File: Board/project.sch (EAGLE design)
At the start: 19 parts, among them U1 ATMEGA328P_PDIP

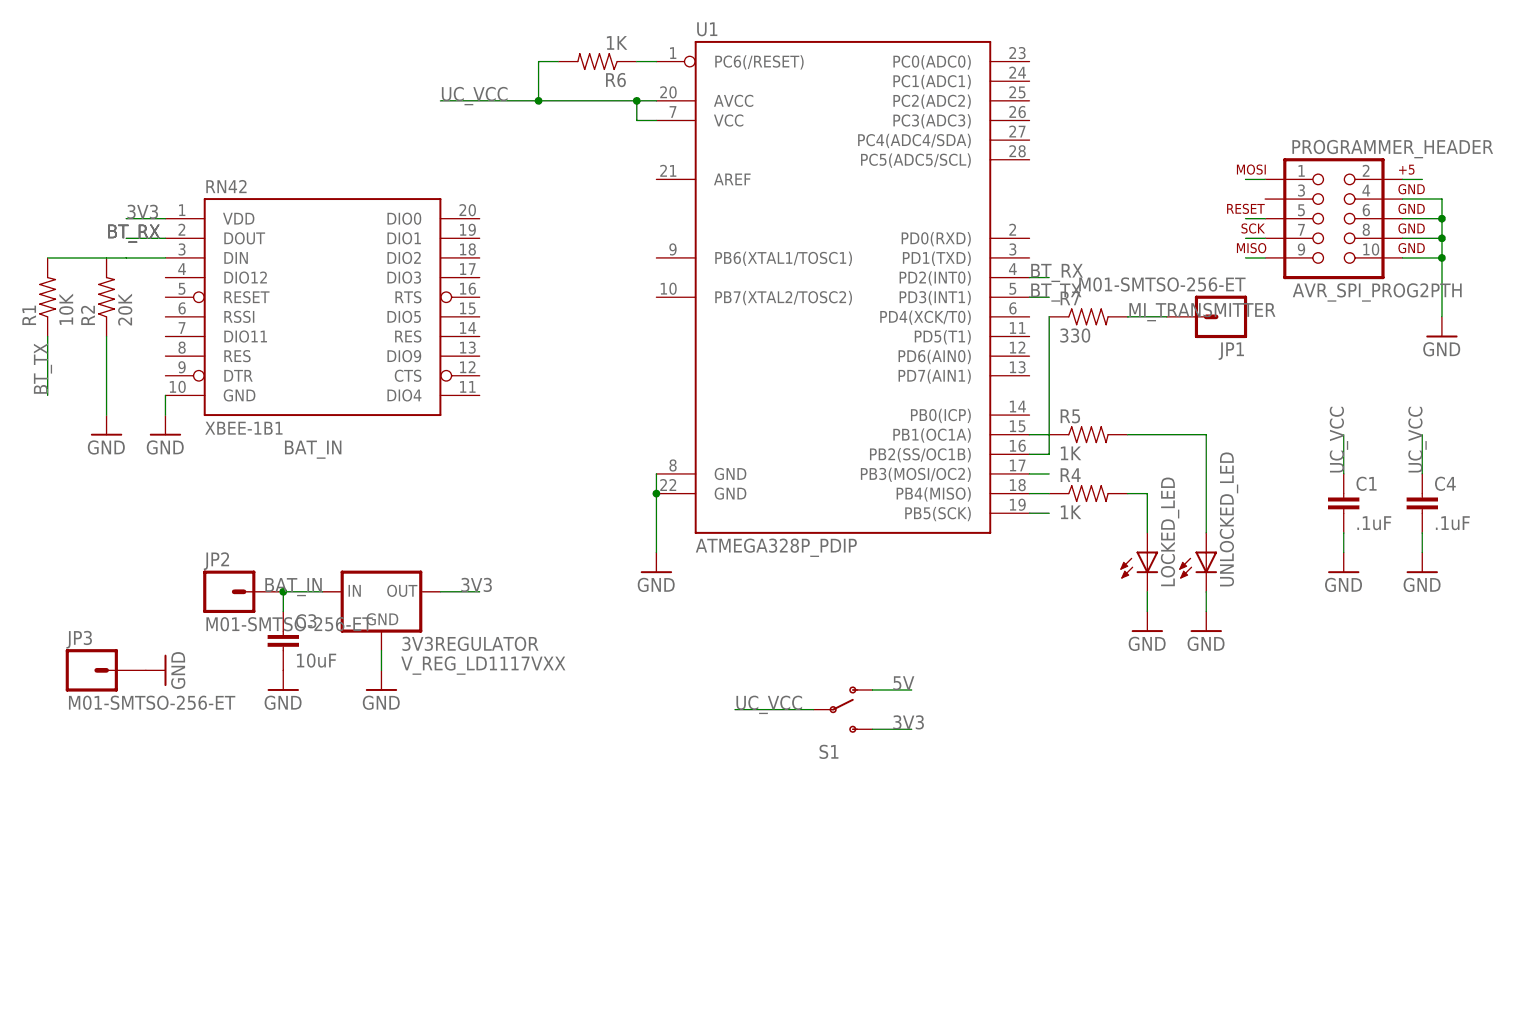
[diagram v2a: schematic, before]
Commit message: Better board layout, everything that needs to be should be connected, passes DRC.
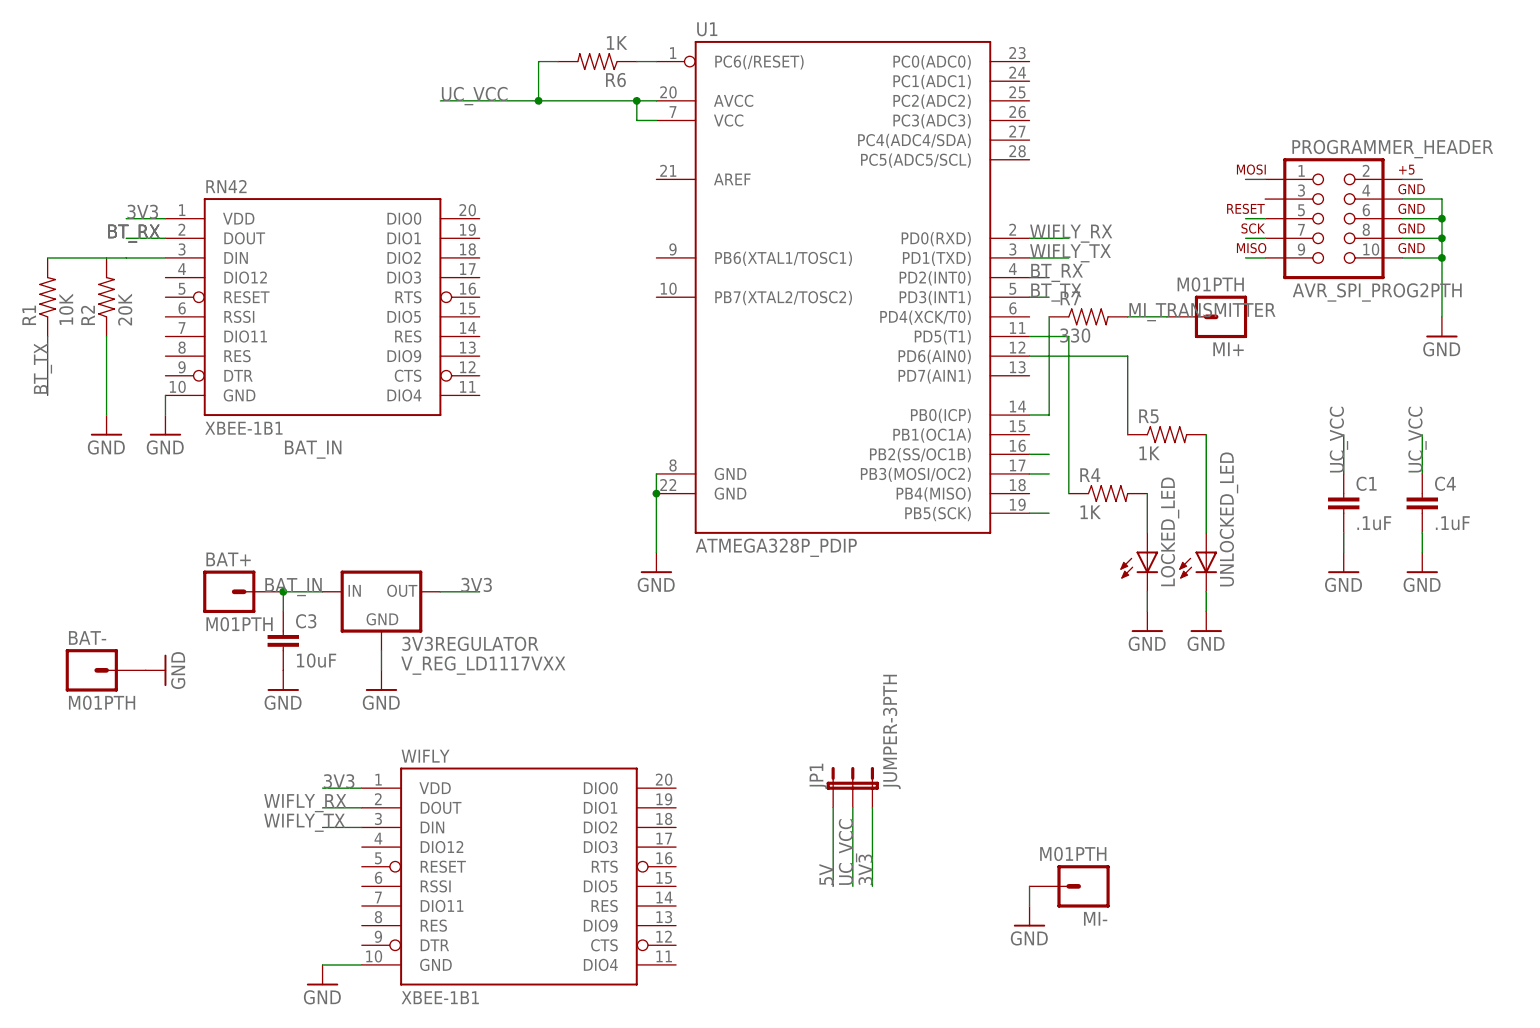
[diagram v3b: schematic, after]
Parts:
- removed JP2, JP3: M01-SMTSO-256-ET, SparkFun-Connectors:M01-SMTSO-256-ET
- removed S1: (no value), SparkFun-Electromechanical:SWITCH-SPDTPTH
- added BAT+, BAT-, MI+, MI-: M01PTH, SparkFun-Connectors:M01PTH
- added WIFLY: XBEE-1B1, SparkFun-RF:XBEE-1B1
- JP1: value M01-SMTSO-256-ET -> JUMPER-3PTH; device SparkFun-Connectors:M01-SMTSO-256-ET -> SparkFun-Passives:JUMPER-3PTH
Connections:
- new net N$4: R4.1, U1.PD5(T1)
- new net N$7: R7.1, U1.PB0(ICP)
- new net WIFLY_RX: U1.PD0(RXD), WIFLY.DOUT
- new net WIFLY_TX: U1.PD1(TXD), WIFLY.DIN
- net 3V3: now also JP1.3, WIFLY.VDD; no longer S1.S
- net 5V: now also JP1.1; no longer S1.O
- net BAT_IN: now also BAT+.1; no longer JP2.1
- net GND: now also BAT-.1, MI-.1, WIFLY.GND; no longer JP3.1
- net MISO: no longer R4.1, U1.PB4(MISO)
- net MI_TRANSMITTER: now also MI+.1; no longer JP1.1
- net N$2: now also U1.PD6(AIN0); no longer U1.PB1(OC1A)
- net N$3: no longer R7.1
- net UC_VCC: no longer S1.P
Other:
- moved on the sheet: R4, R5
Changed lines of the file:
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@@
 <part name="UNLOCKED_LED" library="SparkFun-LED" deviceset="LED" device="5MM"/>
 <part name="LOCKED_LED" library="SparkFun-LED" deviceset="LED" device="5MM"/>
-<part name="S1" library="SparkFun-Electromechanical" deviceset="SWITCH-SPDT" device="PTH"/>
 <part name="GND1" library="SparkFun-Aesthetics" deviceset="GND" device=""/>
 <part name="GND2" library="SparkFun-Aesthetics" deviceset="GND" device=""/>
@@
 <part name="GND9" library="SparkFun-Aesthetics" deviceset="GND" device=""/>
 <part name="GND10" library="SparkFun-Aesthetics" deviceset="GND" device=""/>
-<part name="JP1" library="SparkFun-Connectors" deviceset="M01" device="-SMTSO-256-ET"/>
-<part name="JP2" library="SparkFun-Connectors" deviceset="M01" device="-SMTSO-256-ET"/>
-<part name="JP3" library="SparkFun-Connectors" deviceset="M01" device="-SMTSO-256-ET"/>
 <part name="GND11" library="SparkFun-Aesthetics" deviceset="GND" device=""/>
+<part name="WIFLY" library="SparkFun-RF" deviceset="XBEE-1" device="B1"/>
+<part name="GND12" library="SparkFun-Aesthetics" deviceset="GND" device=""/>
+<part name="BAT+" library="SparkFun-Connectors" deviceset="M01" device="PTH"/>
+<part name="MI+" library="SparkFun-Connectors" deviceset="M01" device="PTH"/>
+<part name="BAT-" library="SparkFun-Connectors" deviceset="M01" device="PTH"/>
+<part name="JP1" library="SparkFun-Passives" deviceset="JUMPER-3" device="PTH"/>
+<part name="MI-" library="SparkFun-Connectors" deviceset="M01" device="PTH"/>
+<part name="GND13" library="SparkFun-Aesthetics" deviceset="GND" device=""/>
 </parts>
 <sheets>
@@
 <instance part="R1" gate="G$1" x="-96.52" y="91.44" rot="R90"/>
 <instance part="R2" gate="G$1" x="-88.9" y="91.44" rot="R90"/>
-<instance part="R4" gate="G$1" x="38.1" y="66.04"/>
-<instance part="R5" gate="G$1" x="38.1" y="73.66"/>
+<instance part="R4" gate="G$1" x="40.64" y="66.04"/>
+<instance part="R5" gate="G$1" x="48.26" y="73.66"/>
 <instance part="R6" gate="G$1" x="-25.4" y="121.92" rot="R180"/>
 <instance part="C1" gate="G$1" x="71.12" y="63.5"/>
@@
 <instance part="UNLOCKED_LED" gate="G$1" x="53.34" y="58.42"/>
 <instance part="LOCKED_LED" gate="G$1" x="45.72" y="58.42"/>
-<instance part="S1" gate="1" x="5.08" y="38.1"/>
 <instance part="GND1" gate="1" x="-17.78" y="55.88"/>
 <instance part="GND2" gate="1" x="-53.34" y="40.64"/>
@@
 <instance part="GND9" gate="1" x="81.28" y="55.88"/>
 <instance part="GND10" gate="1" x="-66.04" y="40.64"/>
-<instance part="JP1" gate="G$1" x="55.88" y="88.9" rot="R180"/>
-<instance part="JP2" gate="G$1" x="-73.66" y="53.34"/>
-<instance part="JP3" gate="G$1" x="-91.44" y="43.18"/>
 <instance part="GND11" gate="1" x="-81.28" y="43.18" rot="R90"/>
+<instance part="WIFLY" gate="G$1" x="-35.56" y="17.78"/>
+<instance part="GND12" gate="1" x="-60.96" y="2.54"/>
+<instance part="BAT+" gate="G$1" x="-73.66" y="53.34"/>
+<instance part="MI+" gate="G$1" x="55.88" y="88.9" rot="R180"/>
+<instance part="BAT-" gate="G$1" x="-91.44" y="43.18"/>
+<instance part="JP1" gate="G$1" x="5.08" y="27.94"/>
+<instance part="MI-" gate="G$1" x="38.1" y="15.24" rot="R180"/>
+<instance part="GND13" gate="1" x="30.48" y="10.16"/>
 </instances>
 <busses>
@@
 </segment>
 <segment>
-<pinref part="JP3" gate="G$1" pin="1"/>
+<pinref part="WIFLY" gate="G$1" pin="GND"/>
+<wire x1="-55.88" y1="5.08" x2="-60.96" y2="5.08" width="0.1524" layer="91"/>
+<pinref part="GND12" gate="1" pin="GND"/>
+</segment>
+<segment>
 <pinref part="GND11" gate="1" pin="GND"/>
+<pinref part="BAT-" gate="G$1" pin="1"/>
+</segment>
+<segment>
+<pinref part="MI-" gate="G$1" pin="1"/>
+<pinref part="GND13" gate="1" pin="GND"/>
+<wire x1="30.48" y1="15.24" x2="30.48" y2="12.7" width="0.1524" layer="91"/>
 </segment>
 </net>
 <net name="UC_VCC" class="0">
 <segment>
-<pinref part="S1" gate="1" pin="P"/>
-<label x="-7.62" y="38.1" size="1.778" layer="95"/>
-<wire x1="2.54" y1="38.1" x2="-7.62" y2="38.1" width="0.1524" layer="91"/>
+<label x="7.62" y="15.24" size="1.778" layer="95" rot="R90"/>
+<wire x1="7.62" y1="25.4" x2="7.62" y2="15.24" width="0.1524" layer="91"/>
 </segment>
 <segment>
@@
 <net name="5V" class="0">
 <segment>
-<pinref part="S1" gate="1" pin="O"/>
-<wire x1="10.16" y1="40.64" x2="15.24" y2="40.64" width="0.1524" layer="91"/>
-<label x="12.7" y="40.64" size="1.778" layer="95"/>
-</segment>
-<segment>
 <pinref part="PROGRAMMER_HEADER" gate="A" pin="2"/>
 <wire x1="78.74" y1="106.68" x2="81.28" y2="106.68" width="0.1524" layer="91"/>
 </segment>
+<segment>
+<pinref part="JP1" gate="G$1" pin="1"/>
+<wire x1="5.08" y1="25.4" x2="5.08" y2="15.24" width="0.1524" layer="91"/>
+<label x="5.08" y="15.24" size="1.778" layer="95" rot="R90"/>
+</segment>
 </net>
 <net name="3V3" class="0">
-<segment>
-<pinref part="S1" gate="1" pin="S"/>
-<wire x1="10.16" y1="35.56" x2="15.24" y2="35.56" width="0.1524" layer="91"/>
-<label x="12.7" y="35.56" size="1.778" layer="95"/>
-</segment>
 <segment>
 <pinref part="3V3REGULATOR" gate="G$1" pin="OUT"/>
@@
 <label x="-86.36" y="101.6" size="1.778" layer="95"/>
 <wire x1="-81.28" y1="101.6" x2="-86.36" y2="101.6" width="0.1524" layer="91"/>
+</segment>
+<segment>
+<pinref part="WIFLY" gate="G$1" pin="VDD"/>
+<wire x1="-55.88" y1="27.94" x2="-60.96" y2="27.94" width="0.1524" layer="91"/>
+<label x="-60.96" y="27.94" size="1.778" layer="95"/>
+</segment>
+<segment>
+<pinref part="JP1" gate="G$1" pin="3"/>
+<wire x1="10.16" y1="25.4" x2="10.16" y2="15.24" width="0.1524" layer="91"/>
+<label x="10.16" y="15.24" size="1.778" layer="95" rot="R90"/>
 </segment>
 </net>
@@
 <label x="-66.04" y="71.12" size="1.778" layer="95"/>
 <label x="-68.58" y="53.34" size="1.778" layer="95"/>
-<pinref part="JP2" gate="G$1" pin="1"/>
+<pinref part="BAT+" gate="G$1" pin="1"/>
 <junction x="-66.04" y="53.34"/>
 </segment>
 </net>
 <net name="MISO" class="0">
-<segment>
-<pinref part="U1" gate="G$1" pin="PB4(MISO)"/>
-<pinref part="R4" gate="G$1" pin="1"/>
-<wire x1="30.48" y1="66.04" x2="33.02" y2="66.04" width="0.1524" layer="91"/>
-</segment>
 <segment>
 <pinref part="PROGRAMMER_HEADER" gate="A" pin="9"/>
@@
 <segment>
 <pinref part="R4" gate="G$1" pin="2"/>
-<wire x1="43.18" y1="66.04" x2="45.72" y2="66.04" width="0.1524" layer="91"/>
 <pinref part="LOCKED_LED" gate="G$1" pin="A"/>
 <wire x1="45.72" y1="66.04" x2="45.72" y2="60.96" width="0.1524" layer="91"/>
@@
 <segment>
 <pinref part="R5" gate="G$1" pin="2"/>
-<wire x1="43.18" y1="73.66" x2="53.34" y2="73.66" width="0.1524" layer="91"/>
 <pinref part="UNLOCKED_LED" gate="G$1" pin="A"/>
 <wire x1="53.34" y1="73.66" x2="53.34" y2="60.96" width="0.1524" layer="91"/>
@@
 <wire x1="43.18" y1="88.9" x2="48.26" y2="88.9" width="0.1524" layer="91"/>
 <label x="43.18" y="88.9" size="1.778" layer="95"/>
-<pinref part="JP1" gate="G$1" pin="1"/>
-</segment>
-</net>
-<net name="N$2" class="0">
-<segment>
-<pinref part="U1" gate="G$1" pin="PB1(OC1A)"/>
-<pinref part="R5" gate="G$1" pin="1"/>
-<wire x1="30.48" y1="73.66" x2="33.02" y2="73.66" width="0.1524" layer="91"/>
+<pinref part="MI+" gate="G$1" pin="1"/>
 </segment>
 </net>
@@
 <pinref part="U1" gate="G$1" pin="PB2(SS/OC1B)"/>
 <wire x1="30.48" y1="71.12" x2="33.02" y2="71.12" width="0.1524" layer="91"/>
+</segment>
+</net>
+<net name="WIFLY_RX" class="0">
+<segment>
+<pinref part="WIFLY" gate="G$1" pin="DOUT"/>
+<wire x1="-55.88" y1="25.4" x2="-60.96" y2="25.4" width="0.1524" layer="91"/>
+<label x="-68.58" y="25.4" size="1.778" layer="95"/>
+</segment>
+<segment>
+<pinref part="U1" gate="G$1" pin="PD0(RXD)"/>
+<wire x1="30.48" y1="99.06" x2="35.56" y2="99.06" width="0.1524" layer="91"/>
+<label x="30.48" y="99.06" size="1.778" layer="95"/>
+</segment>
+</net>
+<net name="WIFLY_TX" class="0">
+<segment>
+<pinref part="WIFLY" gate="G$1" pin="DIN"/>
+<wire x1="-55.88" y1="22.86" x2="-60.96" y2="22.86" width="0.1524" layer="91"/>
+<label x="-68.58" y="22.86" size="1.778" layer="95"/>
+</segment>
+<segment>
+<pinref part="U1" gate="G$1" pin="PD1(TXD)"/>
+<wire x1="30.48" y1="96.52" x2="35.56" y2="96.52" width="0.1524" layer="91"/>
+<label x="30.48" y="96.52" size="1.778" layer="95"/>
+</segment>
+</net>
+<net name="N$2" class="0">
+<segment>
+<pinref part="U1" gate="G$1" pin="PD6(AIN0)"/>
+<wire x1="30.48" y1="83.82" x2="43.18" y2="83.82" width="0.1524" layer="91"/>
+<pinref part="R5" gate="G$1" pin="1"/>
+<wire x1="43.18" y1="83.82" x2="43.18" y2="73.66" width="0.1524" layer="91"/>
+</segment>
+</net>
+<net name="N$4" class="0">
+<segment>
+<pinref part="R4" gate="G$1" pin="1"/>
+<wire x1="35.56" y1="66.04" x2="35.56" y2="86.36" width="0.1524" layer="91"/>
+<pinref part="U1" gate="G$1" pin="PD5(T1)"/>
+<wire x1="35.56" y1="86.36" x2="30.48" y2="86.36" width="0.1524" layer="91"/>
+</segment>
+</net>
+<net name="N$7" class="0">
+<segment>
+<pinref part="U1" gate="G$1" pin="PB0(ICP)"/>
+<wire x1="30.48" y1="76.2" x2="33.02" y2="76.2" width="0.1524" layer="91"/>
 <pinref part="R7" gate="G$1" pin="1"/>
-<wire x1="33.02" y1="71.12" x2="33.02" y2="88.9" width="0.1524" layer="91"/>
-</segment>
-</net>
+<wire x1="33.02" y1="76.2" x2="33.02" y2="88.9" width="0.1524" layer="91"/>
+</segment>
+</net>

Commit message: Layout actually works, added silkscreen.
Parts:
- removed JP1: JUMPER-3PTH, SparkFun-Passives:JUMPER-3PTH
- added JP2: JUMPER-3-OLDPTH, SparkFun-Passives:JUMPER-3-OLDPTH
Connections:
- net 3V3: now also 3V3REGULATOR.IN, JP2.1; no longer 3V3REGULATOR.OUT, JP1.3
- net 5V: now also JP2.3; no longer JP1.1
- net BAT_IN: now also 3V3REGULATOR.GND; no longer 3V3REGULATOR.IN
- net GND: now also 3V3REGULATOR.OUT; no longer 3V3REGULATOR.GND
- net UC_VCC: now also JP2.2
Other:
- moved on the sheet: 3V3REGULATOR
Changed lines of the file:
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@@
 <part name="MI+" library="SparkFun-Connectors" deviceset="M01" device="PTH"/>
 <part name="BAT-" library="SparkFun-Connectors" deviceset="M01" device="PTH"/>
-<part name="JP1" library="SparkFun-Passives" deviceset="JUMPER-3" device="PTH"/>
 <part name="MI-" library="SparkFun-Connectors" deviceset="M01" device="PTH"/>
 <part name="GND13" library="SparkFun-Aesthetics" deviceset="GND" device=""/>
+<part name="JP2" library="SparkFun-Passives" deviceset="JUMPER-3-OLD" device="PTH"/>
 </parts>
 <sheets>
@@
 <instance part="PROGRAMMER_HEADER" gate="A" x="68.58" y="101.6"/>
 <instance part="RN42" gate="G$1" x="-60.96" y="91.44"/>
-<instance part="3V3REGULATOR" gate="G$1" x="-53.34" y="53.34"/>
+<instance part="3V3REGULATOR" gate="G$1" x="-55.88" y="55.88" rot="R90"/>
 <instance part="R1" gate="G$1" x="-96.52" y="91.44" rot="R90"/>
 <instance part="R2" gate="G$1" x="-88.9" y="91.44" rot="R90"/>
@@
 <instance part="MI+" gate="G$1" x="55.88" y="88.9" rot="R180"/>
 <instance part="BAT-" gate="G$1" x="-91.44" y="43.18"/>
-<instance part="JP1" gate="G$1" x="5.08" y="27.94"/>
 <instance part="MI-" gate="G$1" x="38.1" y="15.24" rot="R180"/>
 <instance part="GND13" gate="1" x="30.48" y="10.16"/>
+<instance part="JP2" gate="G$1" x="-7.62" y="30.48"/>
 </instances>
 <busses>
@@
 <junction x="-17.78" y="66.04"/>
 <pinref part="GND1" gate="1" pin="GND"/>
-</segment>
-<segment>
-<pinref part="3V3REGULATOR" gate="G$1" pin="GND"/>
-<pinref part="GND2" gate="1" pin="GND"/>
-<wire x1="-53.34" y1="43.18" x2="-53.34" y2="45.72" width="0.1524" layer="91"/>
 </segment>
 <segment>
@@
 <wire x1="30.48" y1="15.24" x2="30.48" y2="12.7" width="0.1524" layer="91"/>
 </segment>
+<segment>
+<pinref part="GND2" gate="1" pin="GND"/>
+<wire x1="-53.34" y1="43.18" x2="-43.18" y2="53.34" width="0.1524" layer="91"/>
+<wire x1="-43.18" y1="53.34" x2="-43.18" y2="63.5" width="0.1524" layer="91"/>
+<pinref part="3V3REGULATOR" gate="G$1" pin="OUT"/>
+<wire x1="-43.18" y1="63.5" x2="-55.88" y2="63.5" width="0.1524" layer="91"/>
+</segment>
 </net>
 <net name="UC_VCC" class="0">
-<segment>
-<label x="7.62" y="15.24" size="1.778" layer="95" rot="R90"/>
-<wire x1="7.62" y1="25.4" x2="7.62" y2="15.24" width="0.1524" layer="91"/>
-</segment>
 <segment>
 <pinref part="U1" gate="G$1" pin="AVCC"/>
@@
 <label x="81.28" y="68.58" size="1.778" layer="95" rot="R90"/>
 </segment>
+<segment>
+<pinref part="JP2" gate="G$1" pin="2"/>
+<wire x1="-5.08" y1="27.94" x2="-5.08" y2="20.32" width="0.1524" layer="91"/>
+<label x="-5.08" y="17.78" size="1.778" layer="95" rot="R90"/>
+</segment>
 </net>
 <net name="5V" class="0">
@@
 </segment>
 <segment>
-<pinref part="JP1" gate="G$1" pin="1"/>
-<wire x1="5.08" y1="25.4" x2="5.08" y2="15.24" width="0.1524" layer="91"/>
-<label x="5.08" y="15.24" size="1.778" layer="95" rot="R90"/>
+<pinref part="JP2" gate="G$1" pin="3"/>
+<wire x1="-2.54" y1="27.94" x2="-2.54" y2="20.32" width="0.1524" layer="91"/>
+<label x="-2.54" y="22.86" size="1.778" layer="95" rot="R90"/>
 </segment>
 </net>
 <net name="3V3" class="0">
-<segment>
-<pinref part="3V3REGULATOR" gate="G$1" pin="OUT"/>
-<wire x1="-45.72" y1="53.34" x2="-40.64" y2="53.34" width="0.1524" layer="91"/>
-<label x="-43.18" y="53.34" size="1.778" layer="95"/>
-</segment>
 <segment>
 <pinref part="RN42" gate="G$1" pin="VDD"/>
@@
 </segment>
 <segment>
-<pinref part="JP1" gate="G$1" pin="3"/>
-<wire x1="10.16" y1="25.4" x2="10.16" y2="15.24" width="0.1524" layer="91"/>
-<label x="10.16" y="15.24" size="1.778" layer="95" rot="R90"/>
+<pinref part="JP2" gate="G$1" pin="1"/>
+<wire x1="-7.62" y1="27.94" x2="-7.62" y2="20.32" width="0.1524" layer="91"/>
+<label x="-7.62" y="22.86" size="1.778" layer="95" rot="R90"/>
+</segment>
+<segment>
+<pinref part="3V3REGULATOR" gate="G$1" pin="IN"/>
+<wire x1="-55.88" y1="45.72" x2="-55.88" y2="48.26" width="0.1524" layer="91"/>
+<label x="-55.88" y="45.72" size="1.778" layer="95" rot="R90"/>
 </segment>
 </net>
 <net name="BAT_IN" class="0">
 <segment>
-<pinref part="3V3REGULATOR" gate="G$1" pin="IN"/>
-<wire x1="-60.96" y1="53.34" x2="-66.04" y2="53.34" width="0.1524" layer="91"/>
 <pinref part="C3" gate="G$1" pin="1"/>
 <wire x1="-66.04" y1="50.8" x2="-66.04" y2="53.34" width="0.1524" layer="91"/>
@@
 <label x="-68.58" y="53.34" size="1.778" layer="95"/>
 <pinref part="BAT+" gate="G$1" pin="1"/>
+<wire x1="-66.04" y1="53.34" x2="-66.04" y2="66.04" width="0.1524" layer="91"/>
 <junction x="-66.04" y="53.34"/>
-</segment>
-</net>
+<wire x1="-66.04" y1="66.04" x2="-48.26" y2="66.04" width="0.1524" layer="91"/>
+<pinref part="3V3REGULATOR" gate="G$1" pin="GND"/>
+<wire x1="-48.26" y1="66.04" x2="-48.26" y2="55.88" width="0.1524" layer="91"/>
+</segment>
+</net>
